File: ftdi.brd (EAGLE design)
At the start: 26 x 33 mm, 38 parts, among them IC1 MAX481CSA

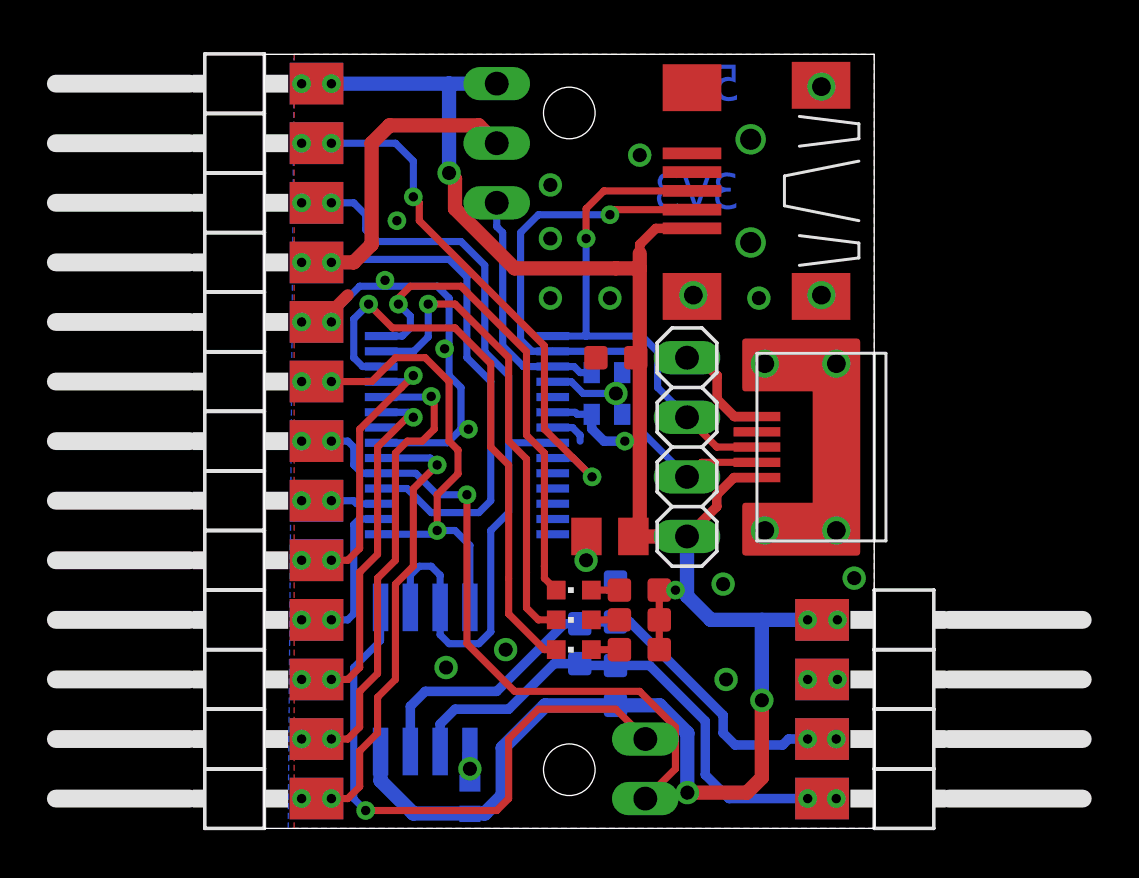
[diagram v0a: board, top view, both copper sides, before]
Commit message: updated libraries and fixed DRC
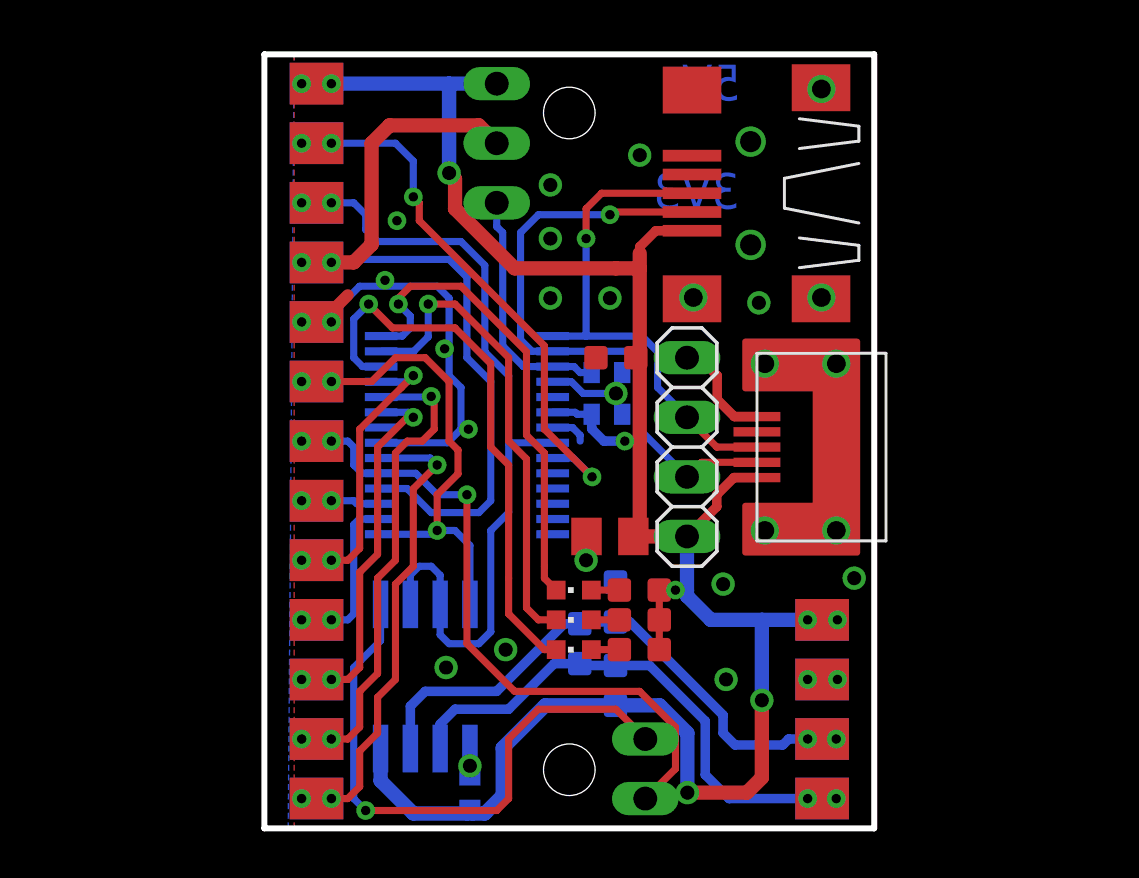
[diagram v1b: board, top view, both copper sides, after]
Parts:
- USBM: value (none) -> USB-MB-S
- moved C5 0.25 mm to (8.76, 1.52)
- moved IC1 0.13 mm to (6.86, 6.48)
- moved USBM 0.10 mm to (20.7, 27.1)
